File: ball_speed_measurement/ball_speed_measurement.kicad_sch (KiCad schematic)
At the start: 14 parts, among them Q1 PMOS, U1 DEV-16771

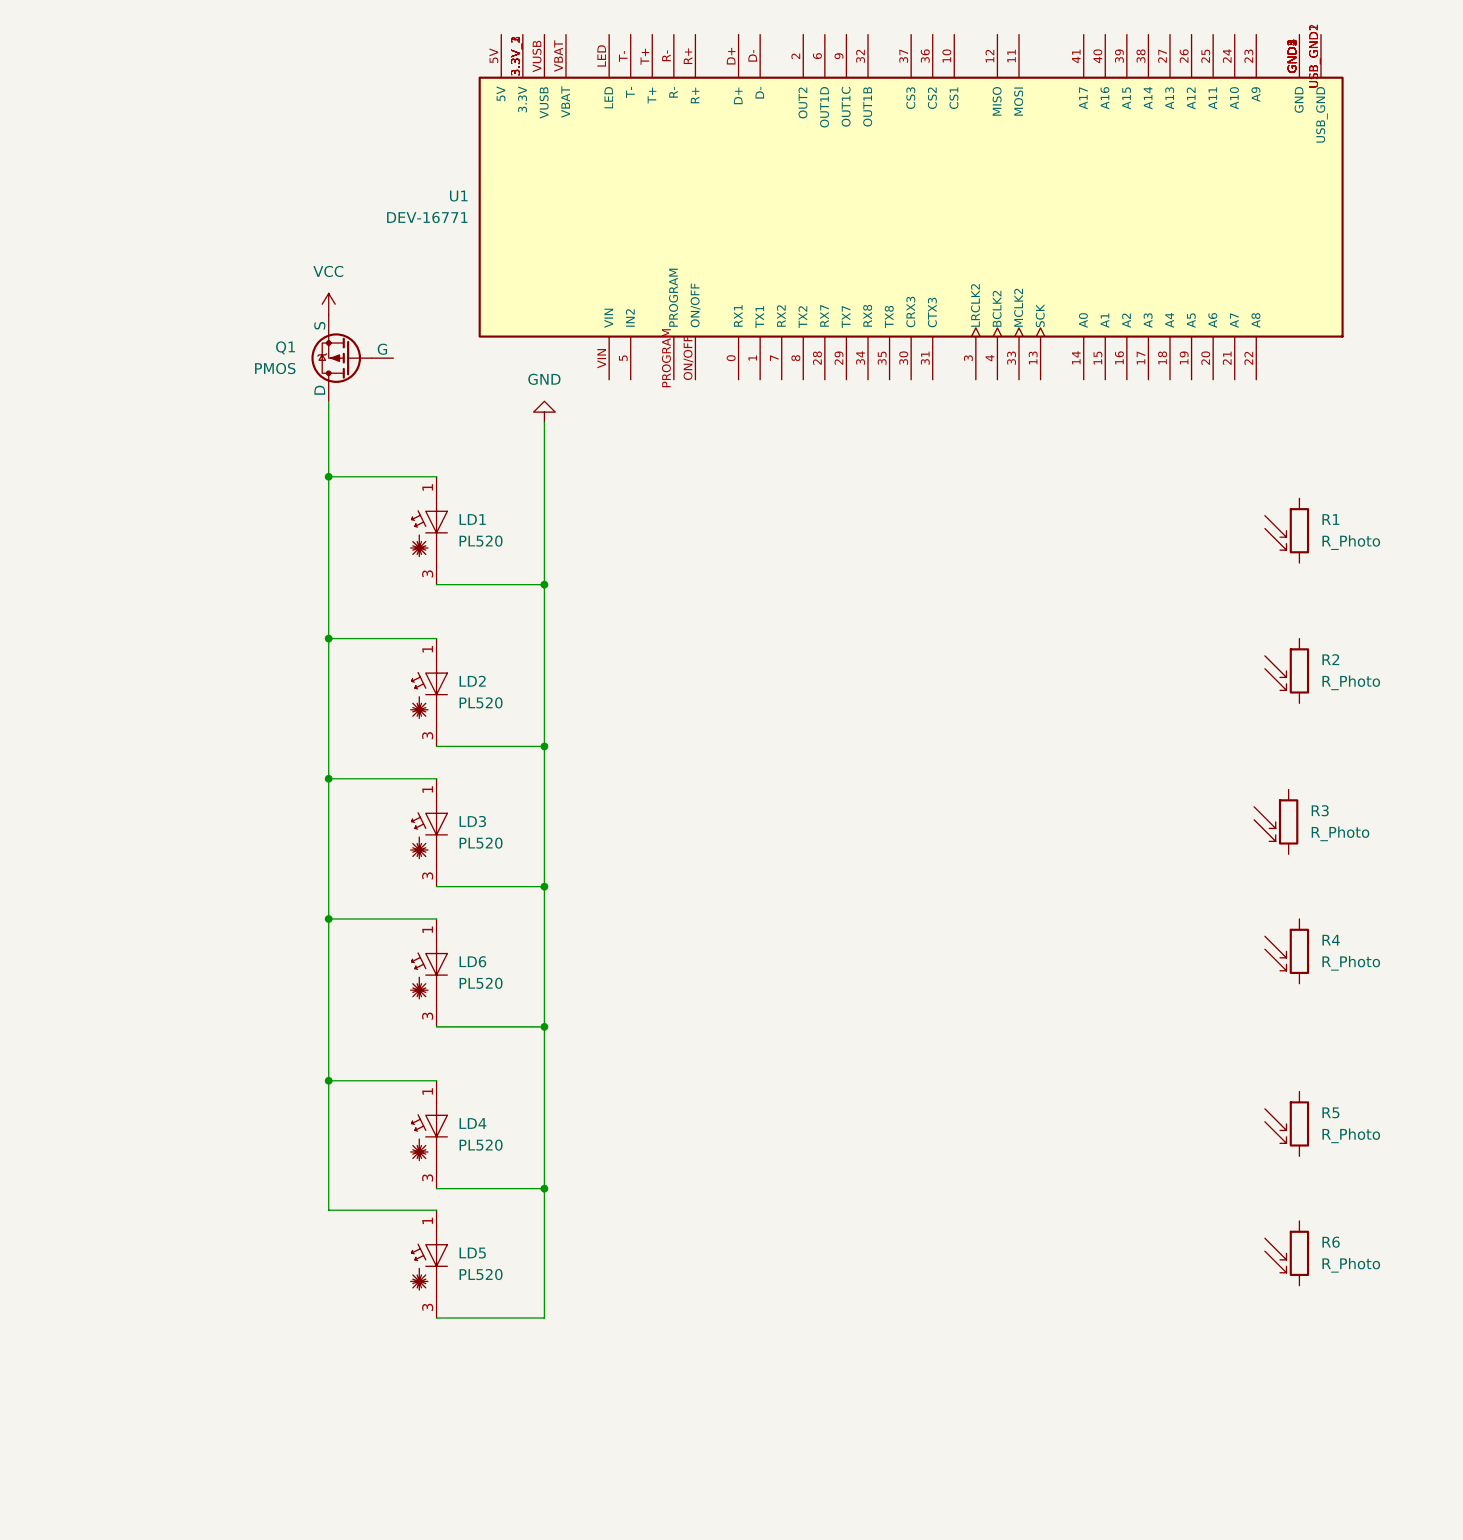
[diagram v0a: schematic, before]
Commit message: First draft of schematic complete
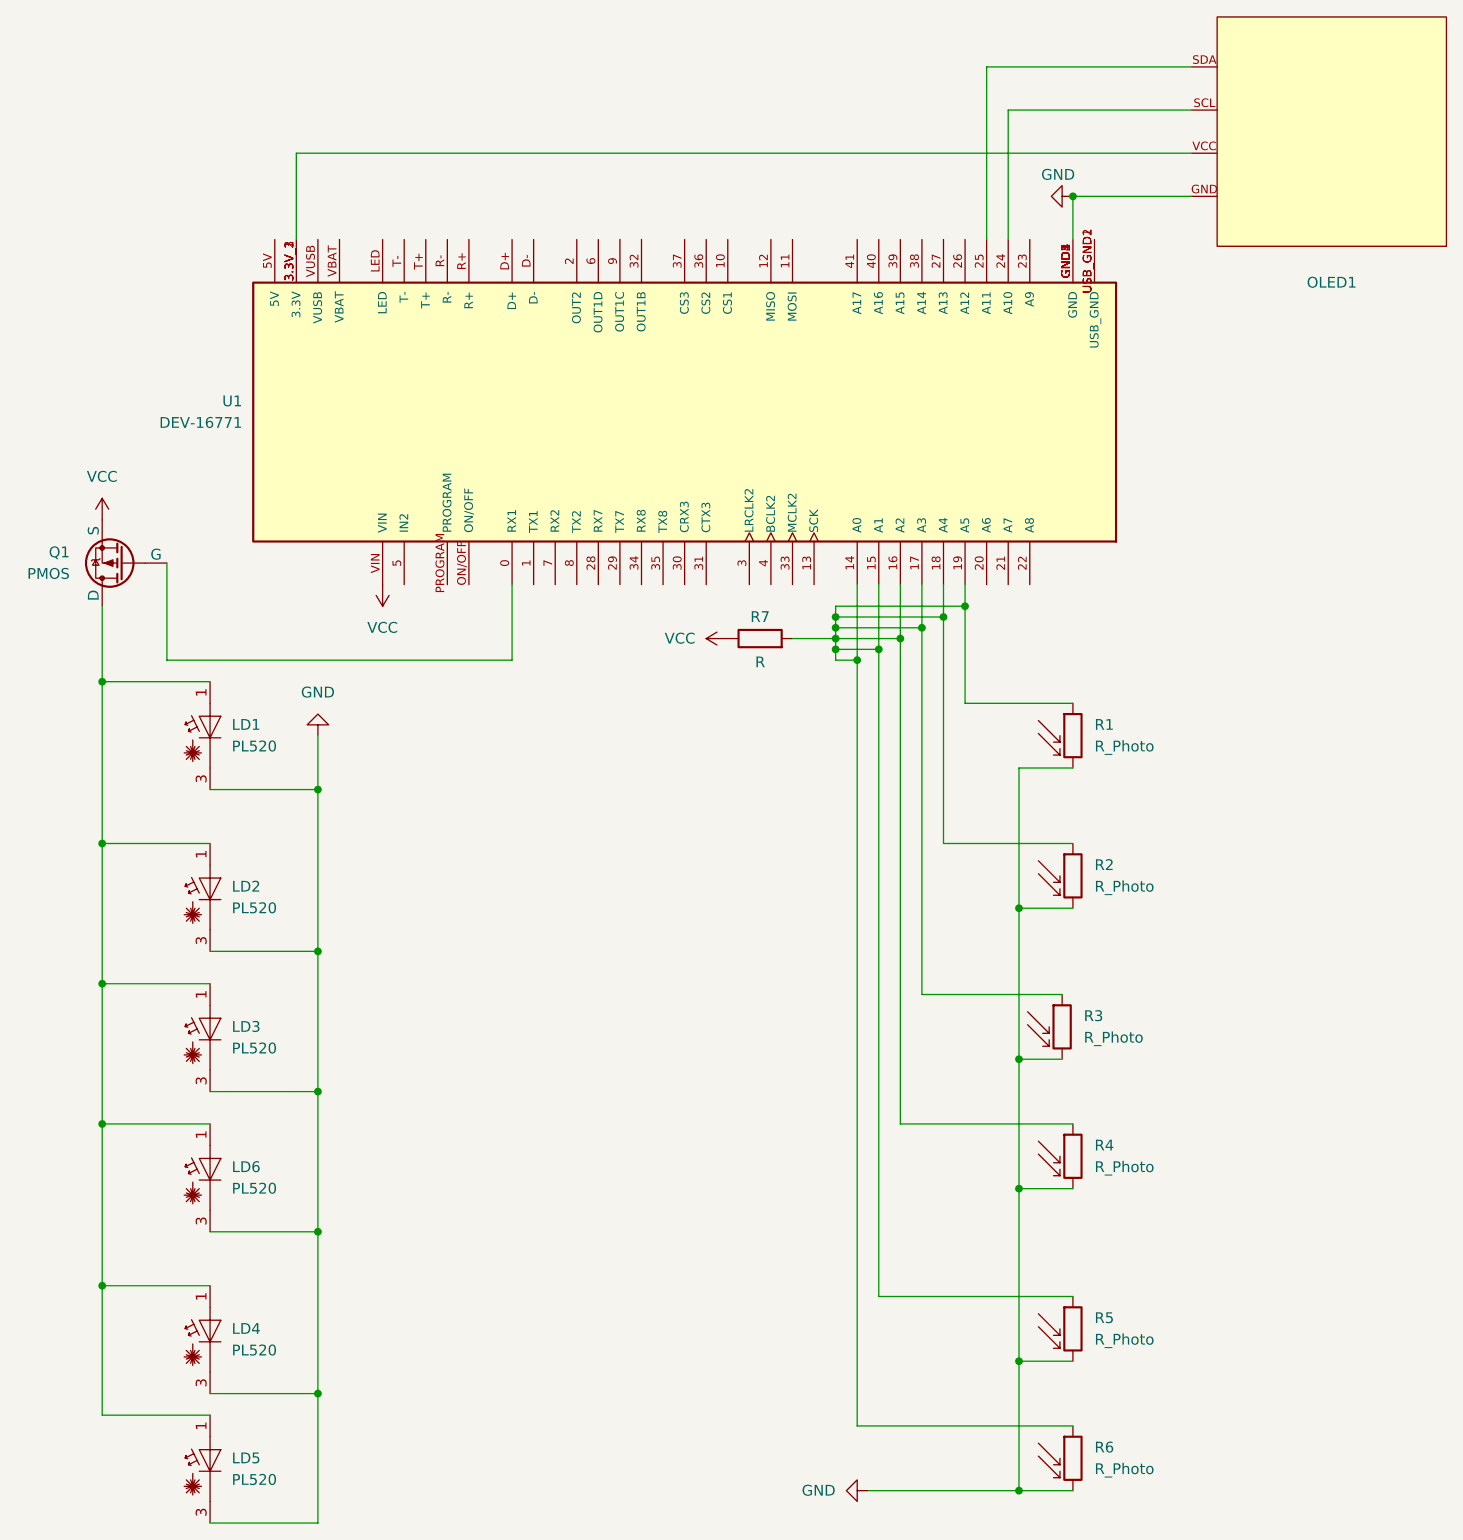
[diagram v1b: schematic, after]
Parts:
- added OLED1: ~, symbol Robocup_Components:OLED_I2C_IIC_Display_Module_12864
- added R7: R, symbol Device:R
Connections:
- net GND: now also R1.2, R2.2, R3.2, R4.2, R5.2, R6.2, U1.GND1 (GND), U1.GND2 (GND), U1.GND3 (GND), U1.GND4 (GND), U1.GND5 (GND), OLED1.GND
- net VCC: now also U1.VIN, R7.1
- net at R5.1: now also R1.1, R2.1, R3.1, R4.1, R6.1, U1.14 (A0), U1.15 (A1), U1.16 (A2), U1.17 (A3), U1.18 (A4), U1.19 (A5), R7.2
- net at Q1.2 (G): now also U1.0 (RX1)
- net at U1.24 (A10): now also OLED1.SCL
- net at U1.25 (A11): now also OLED1.SDA
- net at U1.3.3V_1 (3.3V), U1.3.3V_2 (3.3V), U1.3.3V_3 (3.3V): now also OLED1.VCC
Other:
- moved on the sheet: LD1, LD2, LD3, LD4, LD5, LD6, Q1, R1, R2, R3, R4, R5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

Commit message: Schematic first complete layout, missing resistor values
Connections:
- net GND: now also U1.USB_GND1 (USB_GND), U1.USB_GND2 (USB_GND); no longer LD1.3 (C), LD2.3 (C), LD3.3 (C), LD4.3 (C), LD5.3 (C), LD6.3 (C), OLED1.GND, R1.2, R2.2, R3.2, R4.2, R5.2, R6.2, U1.GND1 (GND), U1.GND2 (GND), U1.GND3 (GND), U1.GND4 (GND), U1.GND5 (GND)
- net VCC: no longer Q1.3 (S), R7.1
- net at OLED1.VCC, U1.3.3V_1 (3.3V), U1.3.3V_2 (3.3V)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: now also R7.1
- new net: OLED1.GND, R1.2, R2.2, R3.2, R4.2, R5.2, R6.2, U1.GND1 (GND), U1.GND2 (GND), U1.GND3 (GND), U1.GND4 (GND), U1.GND5 (GND)
- new net GND Bat.: LD1.3 (C), LD2.3 (C), LD3.3 (C), LD4.3 (C), LD5.3 (C), LD6.3 (C)
- new net VCC Bat.: Q1.3 (S)
